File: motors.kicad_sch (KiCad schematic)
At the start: 6 parts, among them IC2 DRV8836DSSR, J1 Motor A, J2 Motor B

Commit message: work progress
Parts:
- C17: value 220u -> 22u
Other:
- moved on the sheet: C17, C9, IC2, J1, J2

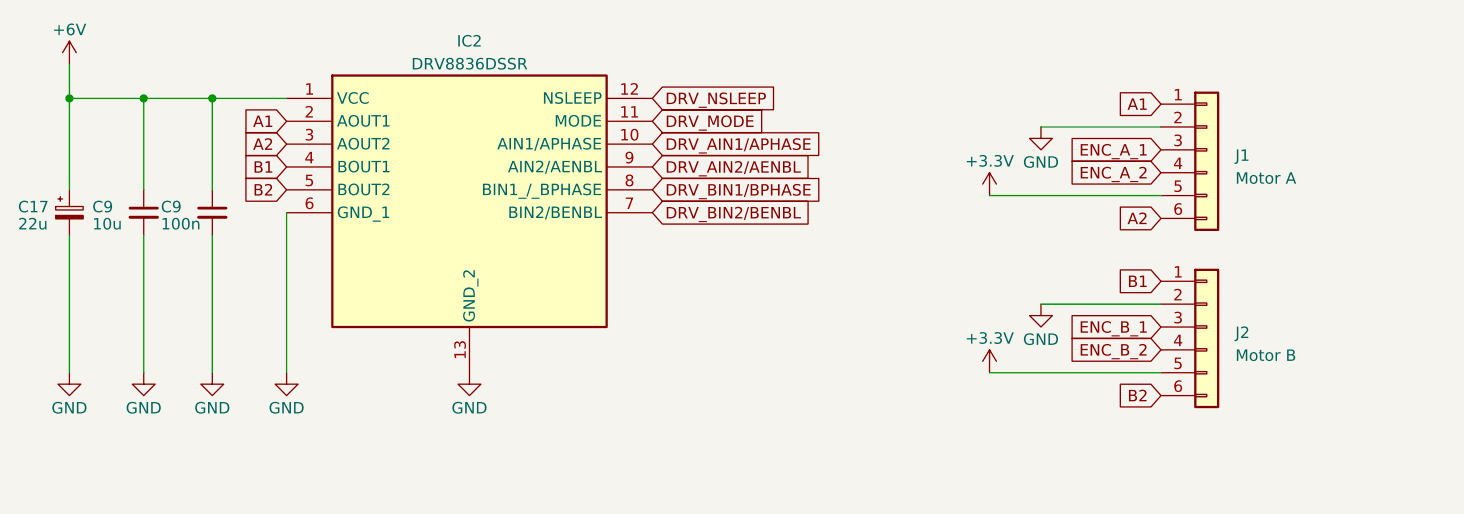
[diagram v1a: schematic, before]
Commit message: most of the components added
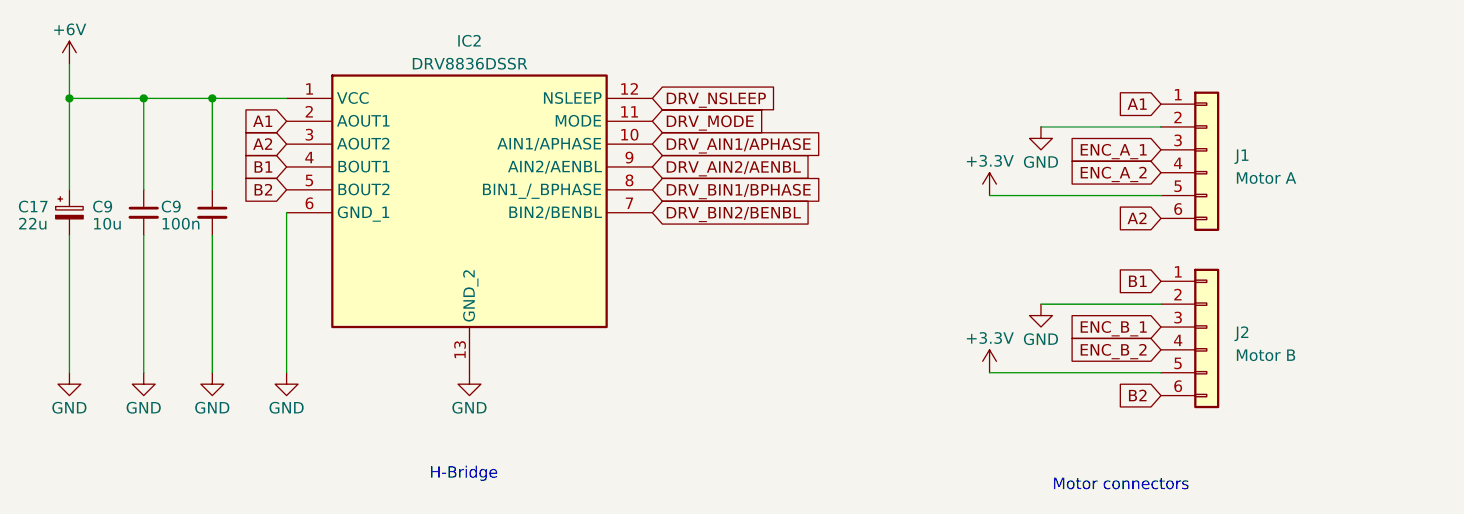
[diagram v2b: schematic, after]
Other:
- note added: "H-Bridge"
- note added: "Motor connectors"
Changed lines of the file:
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@@
     (stroke (width 0) (type default))
+  )
+  (text "H-Bridge" (at 80.645 86.995 0)
+    (effects (font (size 1.27 1.27)) (justify left bottom))
+  )
+  (text "Motor connectors" (at 149.86 88.265 0)
+    (effects (font (size 1.27 1.27)) (justify left bottom))
   )
   (global_label "ENC_B_1" (shape input) (at 161.925 69.85 180) (fields_autoplaced)

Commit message: schematic completed
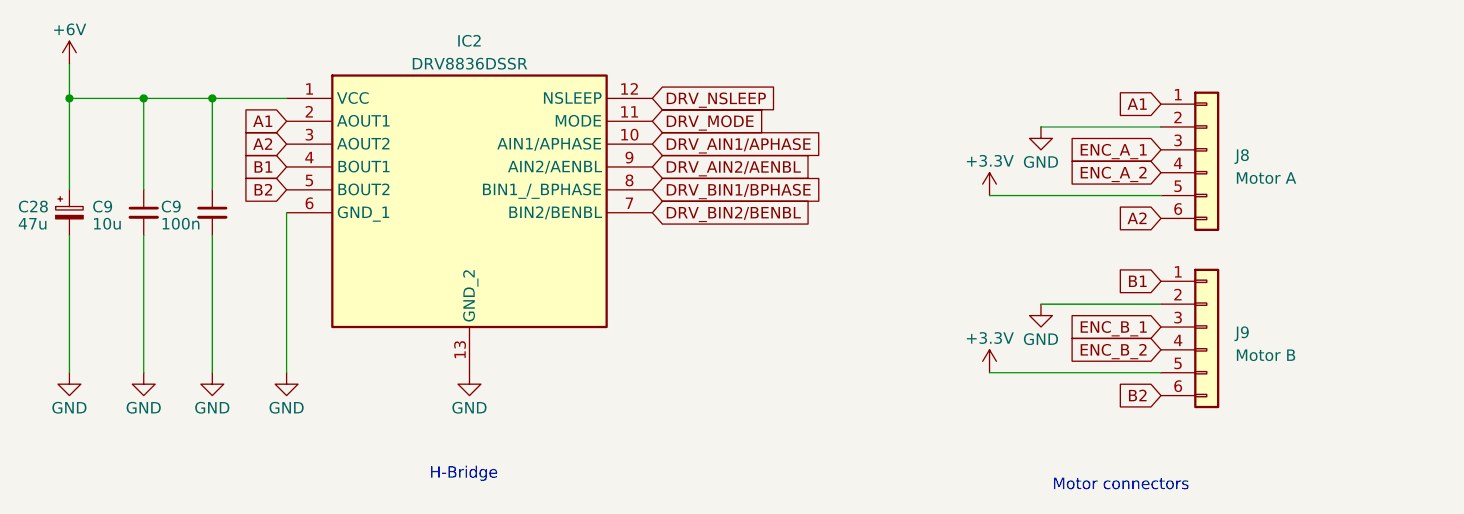
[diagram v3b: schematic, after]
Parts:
- C28: renamed from C17; value 22u -> 47u; footprint (none) -> Capacitor_SMD:CP_Elec_5x5.9
- C9: footprint (none) -> Capacitor_SMD:C_0603_1608Metric
- IC2: footprint SON50P200X300X80-13N-D -> DRV8836DSSR:SON50P200X300X80-13N-D
- renumbered J1 to J8, J2 to J9
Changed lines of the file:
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@@
   (symbol (lib_id "Device:C_Polarized_Small") (at 40.64 57.15 0) (unit 1)
     (in_bom yes) (on_board yes) (dnp no)
-    (property "Reference" "C17" (at 34.925 56.515 0)
-      (effects (font (size 1.27 1.27)) (justify left))
-    )
-    (property "Value" "22u" (at 34.925 58.42 0)
-      (effects (font (size 1.27 1.27)) (justify left))
-    )
-    (property "Footprint" "" (at 40.64 57.15 0)
+    (property "Reference" "C28" (at 34.925 56.515 0)
+      (effects (font (size 1.27 1.27)) (justify left))
+    )
+    (property "Value" "47u" (at 34.925 58.42 0)
+      (effects (font (size 1.27 1.27)) (justify left))
+    )
+    (property "Footprint" "Capacitor_SMD:CP_Elec_5x5.9" (at 40.64 57.15 0)
       (effects (font (size 1.27 1.27)) hide)
     )
@@
       (project "Drv_board"
         (path "/f5f0886f-9115-42d1-ab59-d872f7456d0a/95a79fcf-86f2-4917-a8d6-941d90da7243"
-          (reference "C17") (unit 1)
+          (reference "C28") (unit 1)
         )
       )
@@
         )
         (path "/f5f0886f-9115-42d1-ab59-d872f7456d0a/95a79fcf-86f2-4917-a8d6-941d90da7243"
-          (reference "#PWR043") (unit 1)
+          (reference "#PWR075") (unit 1)
         )
       )
@@
         )
         (path "/f5f0886f-9115-42d1-ab59-d872f7456d0a/95a79fcf-86f2-4917-a8d6-941d90da7243"
-          (reference "#PWR048") (unit 1)
+          (reference "#PWR080") (unit 1)
         )
       )
@@
         )
         (path "/f5f0886f-9115-42d1-ab59-d872f7456d0a/95a79fcf-86f2-4917-a8d6-941d90da7243"
-          (reference "#PWR042") (unit 1)
+          (reference "#PWR077") (unit 1)
         )
       )
@@
   (symbol (lib_id "power:+3.3V") (at 142.875 74.93 0) (unit 1)
     (in_bom yes) (on_board yes) (dnp no) (fields_autoplaced)
-    (property "Reference" "#PWR050" (at 142.875 78.74 0)
+    (property "Reference" "#PWR079" (at 142.875 78.74 0)
       (effects (font (size 1.27 1.27)) hide)
     )
@@
       (project "Drv_board"
         (path "/f5f0886f-9115-42d1-ab59-d872f7456d0a/95a79fcf-86f2-4917-a8d6-941d90da7243"
-          (reference "#PWR050") (unit 1)
+          (reference "#PWR079") (unit 1)
         )
       )
@@
   (symbol (lib_id "power:+3.3V") (at 142.875 55.245 0) (unit 1)
     (in_bom yes) (on_board yes) (dnp no) (fields_autoplaced)
-    (property "Reference" "#PWR047" (at 142.875 59.055 0)
+    (property "Reference" "#PWR078" (at 142.875 59.055 0)
       (effects (font (size 1.27 1.27)) hide)
     )
@@
       (project "Drv_board"
         (path "/f5f0886f-9115-42d1-ab59-d872f7456d0a/95a79fcf-86f2-4917-a8d6-941d90da7243"
-          (reference "#PWR047") (unit 1)
+          (reference "#PWR078") (unit 1)
         )
       )
@@
       (effects (font (size 1.27 1.27)) (justify left))
     )
-    (property "Footprint" "" (at 48.895 57.15 0)
+    (property "Footprint" "Capacitor_SMD:C_0603_1608Metric" (at 48.895 57.15 0)
       (effects (font (size 1.27 1.27)) hide)
     )
@@
         )
         (path "/f5f0886f-9115-42d1-ab59-d872f7456d0a/95a79fcf-86f2-4917-a8d6-941d90da7243"
-          (reference "C16") (unit 1)
+          (reference "C29") (unit 1)
         )
       )
@@
       (effects (font (size 1.27 1.27)) (justify left))
     )
-    (property "Footprint" "" (at 56.515 57.15 0)
+    (property "Footprint" "Capacitor_SMD:C_0603_1608Metric" (at 56.515 57.15 0)
       (effects (font (size 1.27 1.27)) hide)
     )
@@
         )
         (path "/f5f0886f-9115-42d1-ab59-d872f7456d0a/95a79fcf-86f2-4917-a8d6-941d90da7243"
-          (reference "C18") (unit 1)
+          (reference "C30") (unit 1)
         )
       )
@@
         )
         (path "/f5f0886f-9115-42d1-ab59-d872f7456d0a/95a79fcf-86f2-4917-a8d6-941d90da7243"
-          (reference "#PWR044") (unit 1)
+          (reference "#PWR074") (unit 1)
         )
       )
@@
         )
         (path "/f5f0886f-9115-42d1-ab59-d872f7456d0a/95a79fcf-86f2-4917-a8d6-941d90da7243"
-          (reference "#PWR046") (unit 1)
+          (reference "#PWR076") (unit 1)
         )
       )
@@
       (effects (font (size 1.27 1.27)))
     )
-    (property "Footprint" "SON50P200X300X80-13N-D" (at 101.6 139.37 0)
+    (property "Footprint" "DRV8836DSSR:SON50P200X300X80-13N-D" (at 101.6 139.37 0)
       (effects (font (size 1.27 1.27)) (justify left top) hide)
     )
@@
         )
         (path "/f5f0886f-9115-42d1-ab59-d872f7456d0a/95a79fcf-86f2-4917-a8d6-941d90da7243"
-          (reference "#PWR049") (unit 1)
+          (reference "#PWR081") (unit 1)
         )
       )
@@
   (symbol (lib_id "Connector_Generic:Conn_01x06") (at 167.005 69.85 0) (unit 1)
     (in_bom yes) (on_board yes) (dnp no) (fields_autoplaced)
-    (property "Reference" "J2" (at 170.18 70.485 0)
+    (property "Reference" "J9" (at 170.18 70.485 0)
       (effects (font (size 1.27 1.27)) (justify left))
     )
@@
       (project "Drv_board"
         (path "/f5f0886f-9115-42d1-ab59-d872f7456d0a/95a79fcf-86f2-4917-a8d6-941d90da7243"
-          (reference "J2") (unit 1)
+          (reference "J9") (unit 1)
         )
       )
@@
         )
         (path "/f5f0886f-9115-42d1-ab59-d872f7456d0a/95a79fcf-86f2-4917-a8d6-941d90da7243"
-          (reference "#PWR045") (unit 1)
+          (reference "#PWR073") (unit 1)
         )
       )
@@
         )
         (path "/f5f0886f-9115-42d1-ab59-d872f7456d0a/95a79fcf-86f2-4917-a8d6-941d90da7243"
-          (reference "#PWR041") (unit 1)
+          (reference "#PWR072") (unit 1)
         )
       )
@@
   (symbol (lib_id "Connector_Generic:Conn_01x06") (at 167.005 50.165 0) (unit 1)
     (in_bom yes) (on_board yes) (dnp no) (fields_autoplaced)
-    (property "Reference" "J1" (at 170.18 50.8 0)
+    (property "Reference" "J8" (at 170.18 50.8 0)
       (effects (font (size 1.27 1.27)) (justify left))
     )
@@
       (project "Drv_board"
         (path "/f5f0886f-9115-42d1-ab59-d872f7456d0a/95a79fcf-86f2-4917-a8d6-941d90da7243"
-          (reference "J1") (unit 1)
-        )
-      )
+          (reference "J8") (unit 1)
+        )
+      )

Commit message: working on pcb
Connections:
- net B1: now also J9.6 (Pin_6); no longer J9.1 (Pin_1)
- net B2: now also J9.1 (Pin_1); no longer J9.6 (Pin_6)
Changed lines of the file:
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@@
     )
   )
-  (global_label "B1" (shape input) (at 161.925 64.77 180) (fields_autoplaced)
+  (global_label "B1" (shape input) (at 161.925 77.47 180) (fields_autoplaced)
     (effects (font (size 1.27 1.27)) (justify right))
-    (property "Intersheetrefs" "${INTERSHEET_REFS}" (at 156.5397 64.77 0)
+    (property "Intersheetrefs" "${INTERSHEET_REFS}" (at 156.5397 77.47 0)
       (effects (font (size 1.27 1.27)) (justify right) hide)
     )
@@
     )
   )
-  (global_label "B2" (shape input) (at 161.925 77.47 180) (fields_autoplaced)
+  (global_label "B2" (shape input) (at 161.925 64.77 180) (fields_autoplaced)
     (effects (font (size 1.27 1.27)) (justify right))
-    (property "Intersheetrefs" "${INTERSHEET_REFS}" (at 156.5397 77.47 0)
+    (property "Intersheetrefs" "${INTERSHEET_REFS}" (at 156.5397 64.77 0)
       (effects (font (size 1.27 1.27)) (justify right) hide)
     )
@@
         )
         (path "/f5f0886f-9115-42d1-ab59-d872f7456d0a/95a79fcf-86f2-4917-a8d6-941d90da7243"
-          (reference "#PWR075") (unit 1)
+          (reference "#PWR078") (unit 1)
         )
       )
@@
         )
         (path "/f5f0886f-9115-42d1-ab59-d872f7456d0a/95a79fcf-86f2-4917-a8d6-941d90da7243"
+          (reference "#PWR073") (unit 1)
+        )
+      )
+    )
+  )
+  (symbol (lib_id "power:GND") (at 85.09 74.93 0) (unit 1)
+    (in_bom yes) (on_board yes) (dnp no)
+    (property "Reference" "#PWR013" (at 85.09 81.28 0)
+      (effects (font (size 1.27 1.27)) hide)
+    )
+    (property "Value" "GND" (at 85.09 78.867 0)
+      (effects (font (size 1.27 1.27)))
+    )
+    (property "Footprint" "" (at 85.09 74.93 0)
+      (effects (font (size 1.27 1.27)) hide)
+    )
+    (property "Datasheet" "" (at 85.09 74.93 0)
+      (effects (font (size 1.27 1.27)) hide)
+    )
+    (pin "1")
+    (instances
+      (project "Controller_board"
+        (path "/79650e32-6fba-4eaa-902b-d1154ea8c394"
+          (reference "#PWR013") (unit 1)
+        )
+      )
+      (project "Drv_board"
+        (path "/f5f0886f-9115-42d1-ab59-d872f7456d0a"
+          (reference "#PWR019") (unit 1)
+        )
+        (path "/f5f0886f-9115-42d1-ab59-d872f7456d0a/e4c5a70b-512a-4b9f-ab91-b16b9dec5f3c"
+          (reference "#PWR025") (unit 1)
+        )
+        (path "/f5f0886f-9115-42d1-ab59-d872f7456d0a/95a79fcf-86f2-4917-a8d6-941d90da7243"
           (reference "#PWR080") (unit 1)
-        )
-      )
-    )
-  )
-  (symbol (lib_id "power:GND") (at 85.09 74.93 0) (unit 1)
-    (in_bom yes) (on_board yes) (dnp no)
-    (property "Reference" "#PWR013" (at 85.09 81.28 0)
-      (effects (font (size 1.27 1.27)) hide)
-    )
-    (property "Value" "GND" (at 85.09 78.867 0)
-      (effects (font (size 1.27 1.27)))
-    )
-    (property "Footprint" "" (at 85.09 74.93 0)
-      (effects (font (size 1.27 1.27)) hide)
-    )
-    (property "Datasheet" "" (at 85.09 74.93 0)
-      (effects (font (size 1.27 1.27)) hide)
-    )
-    (pin "1")
-    (instances
-      (project "Controller_board"
-        (path "/79650e32-6fba-4eaa-902b-d1154ea8c394"
-          (reference "#PWR013") (unit 1)
-        )
-      )
-      (project "Drv_board"
-        (path "/f5f0886f-9115-42d1-ab59-d872f7456d0a"
-          (reference "#PWR019") (unit 1)
-        )
-        (path "/f5f0886f-9115-42d1-ab59-d872f7456d0a/e4c5a70b-512a-4b9f-ab91-b16b9dec5f3c"
-          (reference "#PWR025") (unit 1)
-        )
-        (path "/f5f0886f-9115-42d1-ab59-d872f7456d0a/95a79fcf-86f2-4917-a8d6-941d90da7243"
-          (reference "#PWR077") (unit 1)
         )
       )
@@
   (symbol (lib_id "power:+3.3V") (at 142.875 74.93 0) (unit 1)
     (in_bom yes) (on_board yes) (dnp no) (fields_autoplaced)
-    (property "Reference" "#PWR079" (at 142.875 78.74 0)
+    (property "Reference" "#PWR081" (at 142.875 78.74 0)
       (effects (font (size 1.27 1.27)) hide)
     )
@@
       (project "Drv_board"
         (path "/f5f0886f-9115-42d1-ab59-d872f7456d0a/95a79fcf-86f2-4917-a8d6-941d90da7243"
-          (reference "#PWR079") (unit 1)
+          (reference "#PWR081") (unit 1)
         )
       )
@@
   (symbol (lib_id "power:+3.3V") (at 142.875 55.245 0) (unit 1)
     (in_bom yes) (on_board yes) (dnp no) (fields_autoplaced)
-    (property "Reference" "#PWR078" (at 142.875 59.055 0)
+    (property "Reference" "#PWR074" (at 142.875 59.055 0)
       (effects (font (size 1.27 1.27)) hide)
     )
@@
       (project "Drv_board"
         (path "/f5f0886f-9115-42d1-ab59-d872f7456d0a/95a79fcf-86f2-4917-a8d6-941d90da7243"
-          (reference "#PWR078") (unit 1)
+          (reference "#PWR074") (unit 1)
         )
       )
@@
         )
         (path "/f5f0886f-9115-42d1-ab59-d872f7456d0a/95a79fcf-86f2-4917-a8d6-941d90da7243"
-          (reference "#PWR074") (unit 1)
+          (reference "#PWR077") (unit 1)
         )
       )
@@
         )
         (path "/f5f0886f-9115-42d1-ab59-d872f7456d0a/95a79fcf-86f2-4917-a8d6-941d90da7243"
-          (reference "#PWR076") (unit 1)
+          (reference "#PWR079") (unit 1)
         )
       )
@@
         )
         (path "/f5f0886f-9115-42d1-ab59-d872f7456d0a/95a79fcf-86f2-4917-a8d6-941d90da7243"
-          (reference "#PWR081") (unit 1)
+          (reference "#PWR075") (unit 1)
         )
       )
@@
         )
         (path "/f5f0886f-9115-42d1-ab59-d872f7456d0a/95a79fcf-86f2-4917-a8d6-941d90da7243"
-          (reference "#PWR073") (unit 1)
-        )
-      )
+          (reference "#PWR076") (unit 1)
+        )
+      )

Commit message: more layout added
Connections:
- net A1: now also J8.6 (Pin_6); no longer J8.1 (Pin_1)
- net A2: now also J8.1 (Pin_1); no longer J8.6 (Pin_6)
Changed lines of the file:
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@@
     )
   )
-  (global_label "A2" (shape input) (at 161.925 57.785 180) (fields_autoplaced)
+  (global_label "A2" (shape input) (at 161.925 45.085 180) (fields_autoplaced)
     (effects (font (size 1.27 1.27)) (justify right))
-    (property "Intersheetrefs" "${INTERSHEET_REFS}" (at 156.7211 57.785 0)
+    (property "Intersheetrefs" "${INTERSHEET_REFS}" (at 156.7211 45.085 0)
       (effects (font (size 1.27 1.27)) (justify right) hide)
     )
@@
     )
   )
-  (global_label "A1" (shape input) (at 161.925 45.085 180) (fields_autoplaced)
+  (global_label "A1" (shape input) (at 161.925 57.785 180) (fields_autoplaced)
     (effects (font (size 1.27 1.27)) (justify right))
-    (property "Intersheetrefs" "${INTERSHEET_REFS}" (at 156.7211 45.085 0)
+    (property "Intersheetrefs" "${INTERSHEET_REFS}" (at 156.7211 57.785 0)
       (effects (font (size 1.27 1.27)) (justify right) hide)
     )
